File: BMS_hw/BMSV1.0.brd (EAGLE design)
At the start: 272 x 60 mm, 178 parts, among them IC1 MC33771BEP, IC2 SFH6156, IC3 MIC28515V1, J2 NTC, X2 87758-1816

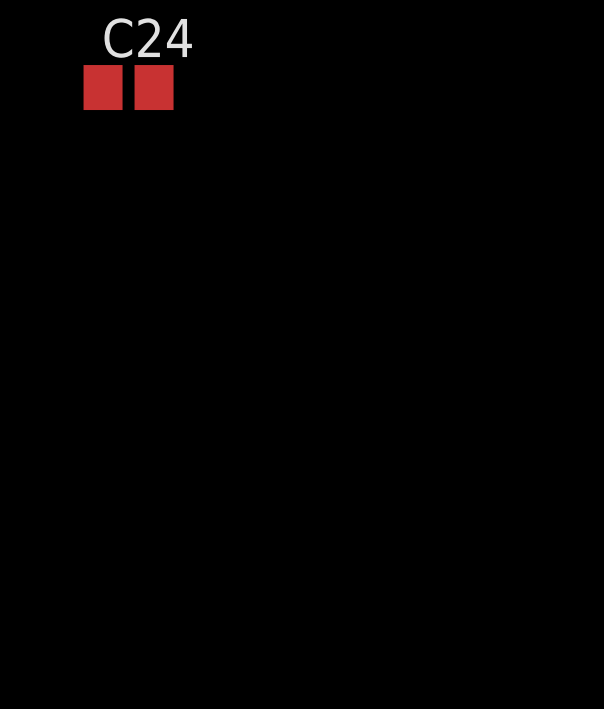
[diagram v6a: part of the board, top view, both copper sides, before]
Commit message: Buck convertor board layout complete routing required!
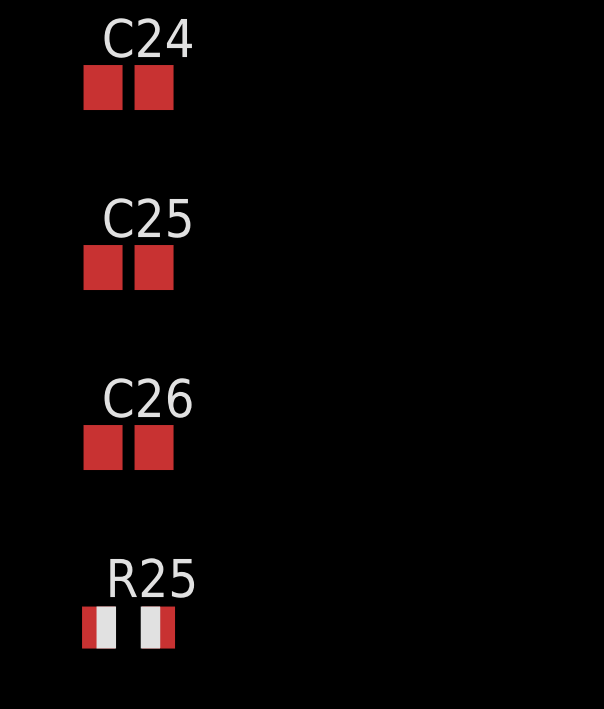
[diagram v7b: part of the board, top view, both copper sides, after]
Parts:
- added C25, C26: 47nF, adafruit:C0805
- added R25: 127E, adafruit:R0805
- C16: value 47nF -> 1uF
- R12: value 127E -> 200k
- R15: value 127E -> 100k
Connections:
- net N$21 renamed VCC
- removed net N$19: IC3.1, R16.1
- removed net N$22: R22.2, R23.1
- removed net PGND: IC3.16, IC3.17, IC3.18, IC3.19, IC3.2, IC3.22, IC3.29
- new net N$21: C26.1, IC3.31, R25.2
- net AGND: no longer IC3.28
- net BST: now also IC3.4
- net FB: now also R22.2, R23.1
- net GND: now also C25.2, C26.2, IC3.17, IC3.18, IC3.19, IC3.22, IC3.28, IC3.29
- net ILIM: now also IC3.1, R16.1
- net N$20: now also IC3.16, IC3.2; no longer IC3.12, IC3.13, IC3.14, IC3.15, IC3.3, R16.2
- net SW: now also IC3.12, IC3.13, IC3.14, IC3.15, IC3.3, R16.2
- net VIN: now also C25.1, R25.1

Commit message: push_11_22_21_09_2018
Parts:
- CELL1+, CELL1-, CELL10+, CELL11+, CELL12+, CELL13+, CELL14+, CELL2+, CELL3+, CELL4+, CELL5+, CELL6+, CELL7+, CELL8+, CELL9+: device GreenFuel:GF-BMS-PAD -> GreenFuel:GF_BMS_CELL_PAD
